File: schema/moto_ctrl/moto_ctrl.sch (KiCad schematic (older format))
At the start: 56 parts

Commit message: Drawing electrical scheme.
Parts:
- removed P?: SETUP, symbol CONN_8
- removed R? (x4): 10k, symbol R
- added K? (x4): CONN_3, symbol CONN_3
- added P?: CONN_2, symbol CONN_2
- added P? (x4): CONN_6, symbol CONN_6
- added R? (x4): 80k, symbol R
- added R? (x12): 10k, symbol R
- added R? (x16): 100, symbol R
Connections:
- net labels added: i-1-1, i-1-2, i-2-1, i-2-2, i-3-1, i-3-2, i-4-1, i-4-2, io-1-1, io-1-2, io-2-1, io-2-2, io-3-1, io-3-2, io-4-1, io-4-2, sensor-1, sensor-2
- net labels removed: addr2, in-scl, in-sda, out-en, out-scl, out-sda, ~in-load, ~in-scl-en, ~out-rst
- wire segments 192 -> 272
- no-connect marks 11 -> 10

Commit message: It looks like it's finished.
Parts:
- added C10, C11, C12, C9: 100n, symbol C
- gave numbers to parts that had none: 92
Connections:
- net labels removed: addr0, addr1
- wire segments 272 -> 286

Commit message: Fixed connection errors.
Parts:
- removed D4: LED, symbol LED
- removed R17: 500, symbol R
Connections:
- net labels added: sensor-3, sensor-4
- net labels removed: led3
- no-connect marks 10 -> 7
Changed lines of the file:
@@
-EESchema Schematic File Version 2  date Mon 05 Nov 2012 01:50:25 PM MSK
+EESchema Schematic File Version 2  date Mon 05 Nov 2012 02:10:58 PM MSK
 LIBS:power
 LIBS:device
@@
 $EndDescr
 Wire Wire Line
+	13950 10200 14500 10200
+Text Label 14100 10200 0    60   ~ 0
+sensor-4
+Text Label 14100 10400 0    60   ~ 0
+sensor-3
+Wire Wire Line
+	13950 10400 14500 10400
+Wire Wire Line
 	27950 3000 27700 3000
 Wire Wire Line
@@
 	1800 8600 1600 8600
 Wire Wire Line
-	2250 6050 2250 5850
-Wire Wire Line
-	2250 6450 2250 6650
-Wire Wire Line
 	1850 6450 1850 6650
 Wire Wire Line
@@
 Wire Wire Line
 	1850 5350 1850 5100
-Wire Wire Line
-	2250 5350 2250 5100
 Wire Wire Line
 	1600 10100 2400 10100
@@
 	13950 8400 14600 8400
 Wire Wire Line
-	13950 10200 15050 10200
-Wire Wire Line
-	13950 9800 15050 9800
+	13950 10000 15050 10000
 Wire Wire Line
 	13950 8600 14600 8600
@@
 	13950 8800 14600 8800
 Wire Wire Line
-	13950 10000 15050 10000
+	13950 9800 15050 9800
 Wire Wire Line
 	8850 8500 9350 8500
@@
 Wire Wire Line
 	25700 3000 25950 3000
+Wire Wire Line
+	9350 6800 8700 6800
+Wire Wire Line
+	9350 7500 8700 7500
+Text Label 8750 7500 0    60   ~ 0
+sensor-2
+Text Label 8750 6800 0    60   ~ 0
+sensor-1
 $Comp
 L GND #PWR01
@@
 	1    0    0    -1
 $EndComp
-NoConn ~ 9350 7500
-NoConn ~ 9350 6800
 Text Label 14500 9600 0    60   ~ 0
 io-4-2
@@
 $EndComp
 Text Label 24700 4000 0    60   ~ 0
-sensor-1
+sensor-3
 $Comp
 L GND #PWR021
@@
 $EndComp
 Text Label 26700 4000 0    60   ~ 0
-sensor-2
+sensor-4
 $Comp
 L GND #PWR025
@@
 Text Label 14450 8800 0    60   ~ 0
 sda
-Text Label 14700 10200 0    60   ~ 0
+Text Label 14700 10000 0    60   ~ 0
 led1
-Text Label 14700 10000 0    60   ~ 0
+Text Label 14700 9800 0    60   ~ 0
 led2
-Text Label 14700 9800 0    60   ~ 0
-led3
 Text Label 14350 8400 0    60   ~ 0
 synch
@@
 NoConn ~ 13950 7100
 NoConn ~ 13950 7300
-NoConn ~ 13950 10400
 $Comp
 L DB9 J1
@@
 synch-ext
 $Comp
-L GND #PWR042
-U 1 1 5096B4B4
-P 2250 6650
-F 0 "#PWR042" H 2250 6650 30  0001 C CNN
-F 1 "GND" H 2250 6580 30  0001 C CNN
-	1    2250 6650
-	1    0    0    -1
-$EndComp
-$Comp
-L R R17
-U 1 1 5096B4B3
-P 2250 5600
-F 0 "R17" V 2330 5600 50  0000 C CNN
-F 1 "500" V 2250 5600 50  0000 C CNN
-	1    2250 5600
-	1    0    0    -1
-$EndComp
-$Comp
-L LED D4
-U 1 1 5096B4B2
-P 2250 6250
-F 0 "D4" H 2250 6350 50  0000 C CNN
-F 1 "LED" H 2250 6150 50  0000 C CNN
-	1    2250 6250
-	0    1    1    0
-$EndComp
-$Comp
 L LED D3
 U 1 1 5096B4B1
@@
 $EndComp
 $Comp
-L GND #PWR043
+L GND #PWR042
 U 1 1 5096B4AF
 P 1850 6650
-F 0 "#PWR043" H 1850 6650 30  0001 C CNN
+F 0 "#PWR042" H 1850 6650 30  0001 C CNN
 F 1 "GND" H 1850 6580 30  0001 C CNN
 	1    1850 6650
 	1    0    0    -1
 $EndComp
-Text Label 2250 5300 1    60   ~ 0
-led3
 Text Label 1850 5300 1    60   ~ 0
 led2
@@
 led1
 $Comp
-L GND #PWR044
+L GND #PWR043
 U 1 1 5096B4AE
 P 1450 6650
-F 0 "#PWR044" H 1450 6650 30  0001 C CNN
+F 0 "#PWR043" H 1450 6650 30  0001 C CNN
 F 1 "GND" H 1450 6580 30  0001 C CNN
 	1    1450 6650
@@
 $EndComp
 $Comp
-L PWR_FLAG #FLG045
+L PWR_FLAG #FLG044
 U 1 1 5096B4AB
 P 1250 12600
-F 0 "#FLG045" H 1250 12695 30  0001 C CNN
+F 0 "#FLG044" H 1250 12695 30  0001 C CNN
 F 1 "PWR_FLAG" H 1250 12780 30  0000 C CNN
 	1    1250 12600
@@
 $EndComp
 $Comp
-L PWR_FLAG #FLG046
+L PWR_FLAG #FLG045
 U 1 1 5096B4AA
 P 1600 12600
-F 0 "#FLG046" H 1600 12695 30  0001 C CNN
+F 0 "#FLG045" H 1600 12695 30  0001 C CNN
 F 1 "PWR_FLAG" H 1600 12780 30  0000 C CNN
 	1    1600 12600
@@
 $EndComp
 $Comp
-L PWR_FLAG #FLG047
+L PWR_FLAG #FLG046
 U 1 1 5096B4A9
 P 1800 15650
-F 0 "#FLG047" H 1800 15745 30  0001 C CNN
+F 0 "#FLG046" H 1800 15745 30  0001 C CNN
 F 1 "PWR_FLAG" H 1800 15830 30  0000 C CNN
 	1    1800 15650
@@
 $EndComp
 $Comp
-L GND #PWR048
+L GND #PWR047
 U 1 1 5096B4A6
 P 2600 17850
-F 0 "#PWR048" H 2600 17850 30  0001 C CNN
+F 0 "#PWR047" H 2600 17850 30  0001 C CNN
 F 1 "GND" H 2600 17780 30  0001 C CNN
 	1    2600 17850
@@
 $EndComp
 $Comp
-L GND #PWR049
+L GND #PWR048
 U 1 1 5096B4A5
 P 1550 18050
-F 0 "#PWR049" H 1550 18050 30  0001 C CNN
+F 0 "#PWR048" H 1550 18050 30  0001 C CNN
 F 1 "GND" H 1550 17980 30  0001 C CNN
 	1    1550 18050
@@
 swd-clk
 $Comp
-L GND #PWR050
+L GND #PWR049
 U 1 1 5096B49F
 P 1250 12800
-F 0 "#PWR050" H 1250 12800 30  0001 C CNN
+F 0 "#PWR049" H 1250 12800 30  0001 C CNN
 F 1 "GND" H 1250 12730 30  0001 C CNN
 	1    1250 12800
@@
 $EndComp
 $Comp
-L VDD #PWR051
+L VDD #PWR050
 U 1 1 5096B49E
 P 1800 12600
-F 0 "#PWR051" H 1800 12700 30  0001 C CNN
+F 0 "#PWR050" H 1800 12700 30  0001 C CNN
 F 1 "VDD" H 1800 12710 30  0000 C CNN
 	1    1800 12600
@@
 $EndComp
 $Comp
-L VDD #PWR052
+L VDD #PWR051
 U 1 1 5096B49C
 P 1800 8500
-F 0 "#PWR052" H 1800 8600 30  0001 C CNN
+F 0 "#PWR051" H 1800 8600 30  0001 C CNN
 F 1 "VDD" H 1800 8610 30  0000 C CNN
 	1    1800 8500
@@
 $EndComp
 $Comp
-L VDD #PWR053
+L VDD #PWR052
 U 1 1 5096B492
 P 1700 9250
-F 0 "#PWR053" H 1700 9350 30  0001 C CNN
+F 0 "#PWR052" H 1700 9350 30  0001 C CNN
 F 1 "VDD" H 1700 9360 30  0000 C CNN
 	1    1700 9250
@@
 $EndComp
 $Comp
-L VDD #PWR054
+L VDD #PWR053
 U 1 1 5096B491
 P 1950 9250
-F 0 "#PWR054" H 1950 9350 30  0001 C CNN
+F 0 "#PWR053" H 1950 9350 30  0001 C CNN
 F 1 "VDD" H 1950 9360 30  0000 C CNN
 	1    1950 9250
@@
 $EndComp
 $Comp
-L VDD #PWR055
+L VDD #PWR054
 U 1 1 5096B48B
 P 2200 9250
-F 0 "#PWR055" H 2200 9350 30  0001 C CNN
+F 0 "#PWR054" H 2200 9350 30  0001 C CNN
 F 1 "VDD" H 2200 9360 30  0000 C CNN
 	1    2200 9250
@@
 $EndComp
 $Comp
-L GND #PWR056
+L GND #PWR055
 U 1 1 5096B480
 P 3500 14250
-F 0 "#PWR056" H 3500 14250 30  0001 C CNN
+F 0 "#PWR055" H 3500 14250 30  0001 C CNN
 F 1 "GND" H 3500 14180 30  0001 C CNN
 	1    3500 14250
@@
 tx
 $Comp
-L PWR_FLAG #FLG057
+L PWR_FLAG #FLG056
 U 1 1 5096B479
 P 2100 12600
-F 0 "#FLG057" H 2100 12695 30  0001 C CNN
+F 0 "#FLG056" H 2100 12695 30  0001 C CNN
 F 1 "PWR_FLAG" H 2100 12780 30  0000 C CNN
 	1    2100 12600
@@
 $EndComp
 $Comp
-L +24V #PWR058
+L +24V #PWR057
 U 1 1 5096B478
 P 2300 12600
-F 0 "#PWR058" H 2300 12550 20  0001 C CNN
+F 0 "#PWR057" H 2300 12550 20  0001 C CNN
 F 1 "+24V" H 2300 12700 30  0000 C CNN
 	1    2300 12600
@@
 synch
 $Comp
-L GND #PWR059
+L GND #PWR058
 U 1 1 5096B3DA
 P 2400 3500
-F 0 "#PWR059" H 2400 3500 30  0001 C CNN
+F 0 "#PWR058" H 2400 3500 30  0001 C CNN
 F 1 "GND" H 2400 3430 30  0001 C CNN
 	1    2400 3500
@@
 $EndComp
 $Comp
-L GND #PWR060
+L GND #PWR059
 U 1 1 5096B3D3
 P 3900 2100
-F 0 "#PWR060" H 3900 2100 30  0001 C CNN
+F 0 "#PWR059" H 3900 2100 30  0001 C CNN
 F 1 "GND" H 3900 2030 30  0001 C CNN
 	1    3900 2100
@@
 $EndComp
 $Comp
-L GND #PWR061
+L GND #PWR060
 U 1 1 5096B3D2
 P 4150 2600
-F 0 "#PWR061" H 4150 2600 30  0001 C CNN
+F 0 "#PWR060" H 4150 2600 30  0001 C CNN
 F 1 "GND" H 4150 2530 30  0001 C CNN
 	1    4150 2600
@@
 $EndComp
 $Comp
-L GND #PWR062
+L GND #PWR061
 U 1 1 5096B3CF
 P 4500 2600
-F 0 "#PWR062" H 4500 2600 30  0001 C CNN
+F 0 "#PWR061" H 4500 2600 30  0001 C CNN
 F 1 "GND" H 4500 2530 30  0001 C CNN
 	1    4500 2600
@@
 $EndComp
 $Comp
-L GND #PWR063
+L GND #PWR062
 U 1 1 5096B3CD
 P 5200 2600
-F 0 "#PWR063" H 5200 2600 30  0001 C CNN
+F 0 "#PWR062" H 5200 2600 30  0001 C CNN
 F 1 "GND" H 5200 2530 30  0001 C CNN
 	1    5200 2600
@@
 $EndComp
 $Comp
-L GND #PWR064
+L GND #PWR063
 U 1 1 5096B3CB
 P 5500 2600
-F 0 "#PWR064" H 5500 2600 30  0001 C CNN
+F 0 "#PWR063" H 5500 2600 30  0001 C CNN
 F 1 "GND" H 5500 2530 30  0001 C CNN
 	1    5500 2600
@@
 $EndComp
 $Comp
-L GND #PWR065
+L GND #PWR064
 U 1 1 5096B3C9
 P 1550 4050
-F 0 "#PWR065" H 1550 4050 30  0001 C CNN
+F 0 "#PWR064" H 1550 4050 30  0001 C CNN
 F 1 "GND" H 1550 3980 30  0001 C CNN
 	1    1550 4050
@@
 3v3-out
 $Comp
-L +24V #PWR066
+L +24V #PWR065
 U 1 1 5096B3C7
 P 950 1450
-F 0 "#PWR066" H 950 1400 20  0001 C CNN
+F 0 "#PWR065" H 950 1400 20  0001 C CNN
 F 1 "+24V" H 950 1550 30  0000 C CNN
 	1    950  1450
@@
 $EndComp
 $Comp
-L VDD #PWR067
+L VDD #PWR066
 U 1 1 5096B3C6
 P 6400 1550
-F 0 "#PWR067" H 6400 1650 30  0001 C CNN
+F 0 "#PWR066" H 6400 1650 30  0001 C CNN
 F 1 "VDD" H 6400 1660 30  0000 C CNN
 	1    6400 1550

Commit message: Fixed error in inductive sensor routing.
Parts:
- added R26, R33, R42, R61: 100, symbol R
- R27: renamed from R6; value 80k -> 81k
- R36: renamed from R7; value 80k -> 81k
- R45: renamed from R8; value 80k -> 81k
- renumbered C5 to C1, C1 to C10, C2 to C11, C3 to C12, C4 to C13, C9 to C14, C10 to C15, C11 to C16, C12 to C17, C13 to C2, C14 to C3, C6 to C4, C7 to C5, C8 to C6, C16 to C7, C17 to C8, C15 to C9, D2 to D1, D3 to D2, D1 to D3, K5 to K1, K1 to K2, K2 to K3, K3 to K4, K4 to K5, P5 to P1, P6 to P2, P1 to P3, P2 to P4, P3 to P5, P4 to P6, R15 to R1, R57 to R10, R47 to R11, R51 to R12, R54 to R13, R55 to R14, R5 to R15, R52 to R16, R53 to R17, R48 to R18, R49 to R19, R1 to R2, R50 to R20, R4 to R21, R43 to R22, R44 to R23, R18 to R24, R10 to R25, R11 to R28, R35 to R29, R58 to R3, R39 to R30, R27 to R31, R31 to R32, R19 to R34, R20 to R35, R12 to R37, R36 to R38, R40 to R39, R45 to R4, R28 to R40, R32 to R41, R21 to R43, R22 to R44, R13 to R46, R37 to R47, R41 to R48, R33 to R49, R2 to R5, R23 to R50, R24 to R51, R29 to R52, R9 to R53, R14 to R54, R38 to R55, R42 to R56, R30 to R57, R34 to R58, R25 to R59, R16 to R6, R26 to R60, R3 to R7, R46 to R8, R56 to R9
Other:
- moved on the sheet: C14, C15, C16, C17, K2, K3, K4, K5, R27, R28, R36, R37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

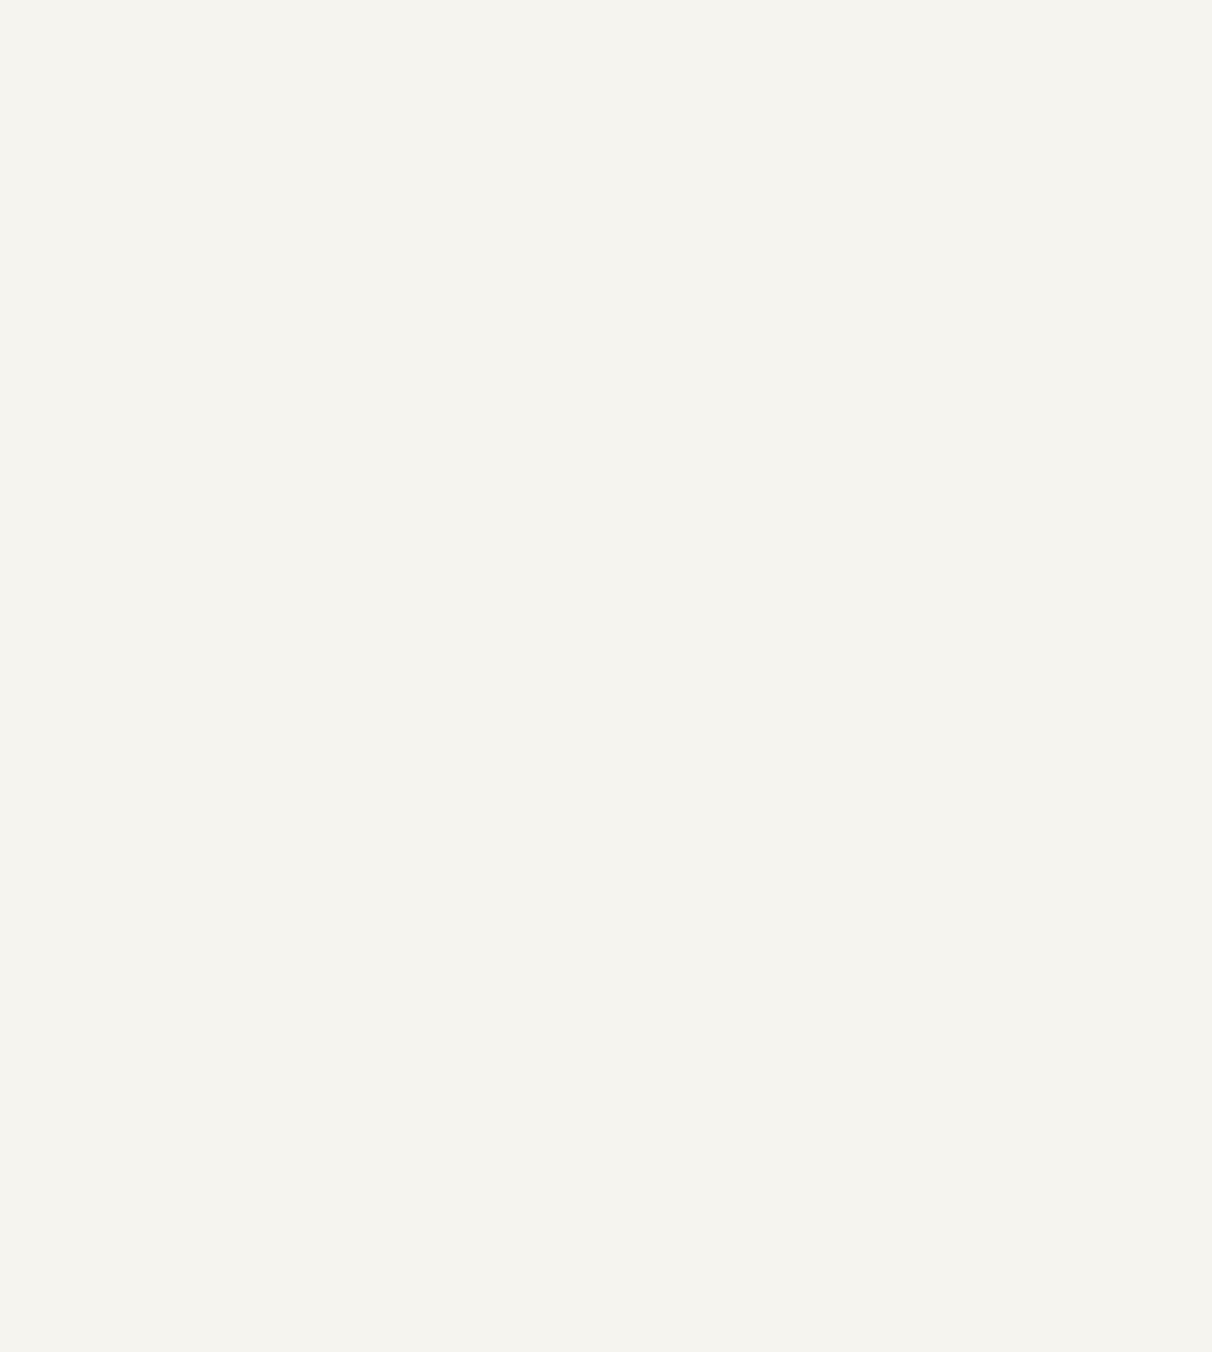
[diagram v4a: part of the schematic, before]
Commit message: Added accelerometer-magnetometer-thermometer in lga14 package.
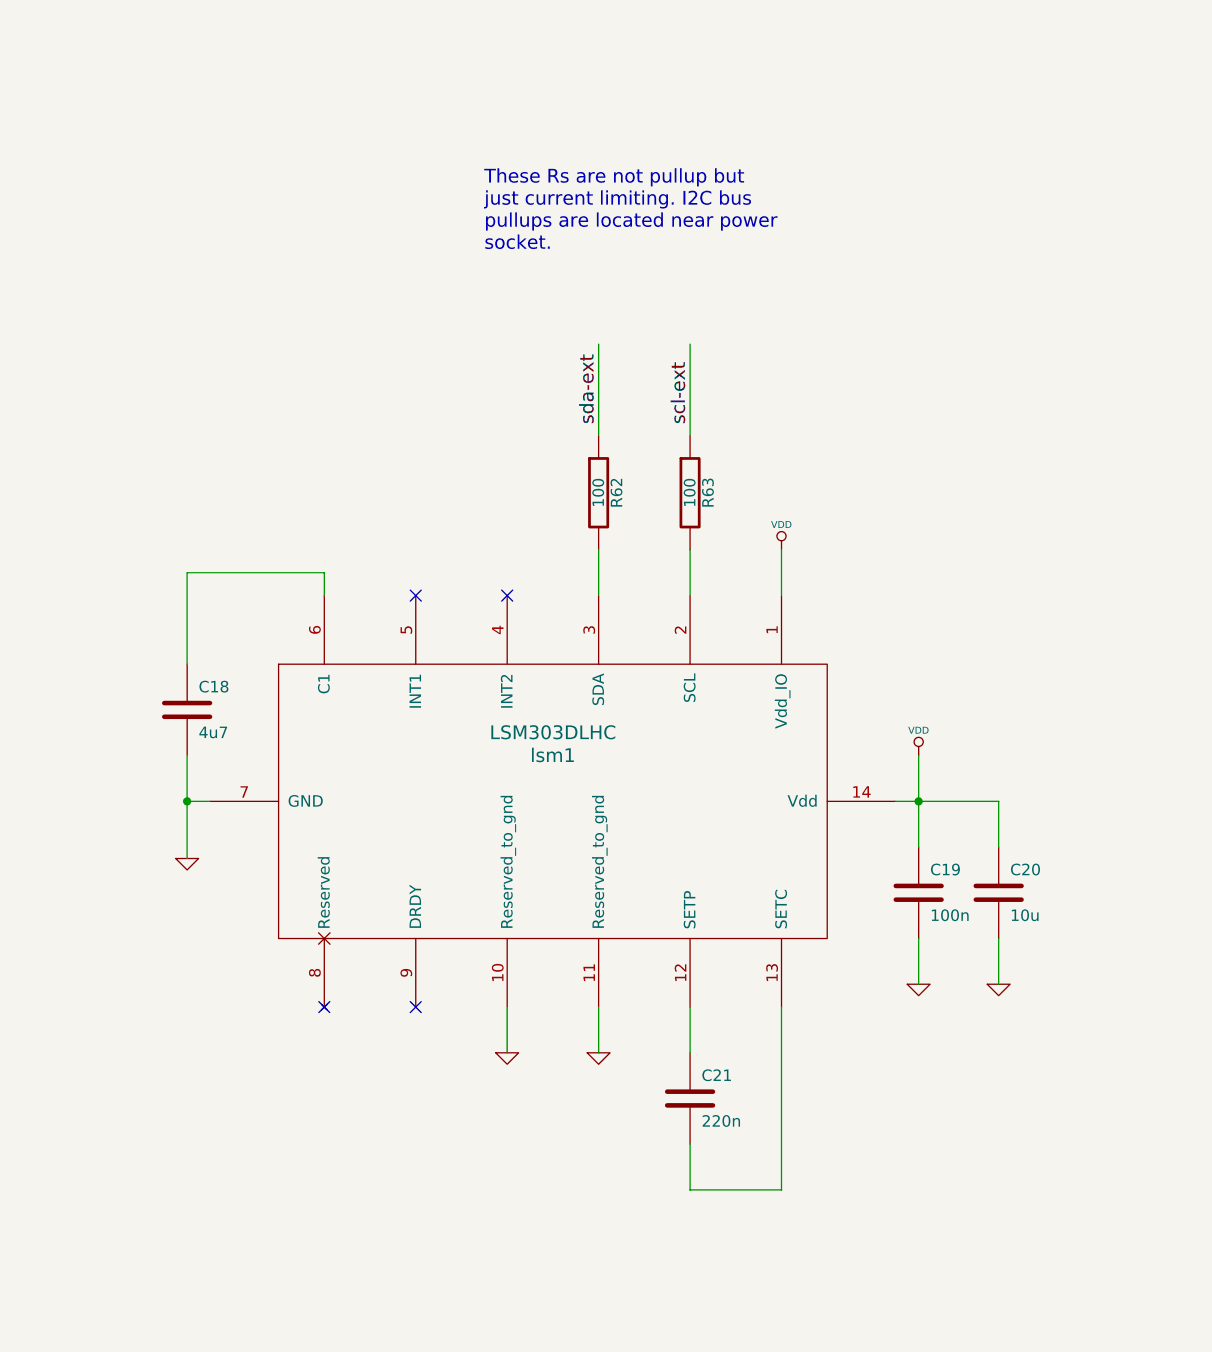
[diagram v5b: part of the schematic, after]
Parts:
- added C18: 4u7, symbol C
- added C19: 100n, symbol C
- added C20: 10u, symbol C
- added C21: 220n, symbol C
- added R62, R63: 100, symbol R
- added lsm1: LSM303DLHC, symbol LSM303DLHC
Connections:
- wire segments 286 -> 307
- no-connect marks 7 -> 11
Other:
- note added: "These Rs are not pullup but \njust current limiting. I2C bus \npullups are located near power \nsocket."

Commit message: Little clemma sockets are replaced with one D-SUB-37.
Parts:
- removed K2, K3, K4, K5: CONN_3, symbol CONN_3
- removed P3, P4, P5, P6: CONN_6, symbol CONN_6
- added J2: DB37, symbol DB37
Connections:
- net labels added: dr-gnd-1, dr-gnd-2, dr-gnd-3, dr-gnd-4, dr-i-11, dr-i-12, dr-i-21, dr-i-22, dr-i-31, dr-i-32, dr-i-41, dr-i-42, dr-io-11, dr-io-12, dr-io-21, dr-io-22, dr-io-31, dr-io-32, dr-io-41, dr-io-42, sen-1, sen-2, sen-3, sen-4, sen-gnd-1, sen-gnd-2, sen-gnd-3, sen-gnd-4, sen-vdd-1, sen-vdd-2, sen-vdd-3, sen-vdd-4
- wire segments 307 -> 339
- no-connect marks 11 -> 12
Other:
- moved on the sheet: R29, R30, R31, R32, R34, R35, R38, R39, R40, R41, R43, R44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
